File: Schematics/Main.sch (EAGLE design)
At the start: 12 parts, among them IC1 PIC12F1840, IC2 7805TV, Q1 BD139, X1 Fan, X2 Power

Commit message: All working now
Issues with repo resolved, back to normal!

Signed-off-by: Aljaž Srebrnič <a2piratesoft@gmail.com>
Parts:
- Q1: device transistor:-NPN-TO126 -> transistor-power:BD139
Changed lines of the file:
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@@
 <layers>
 <layer number="1" name="Top" color="4" fill="1" visible="no" active="no"/>
+<layer number="2" name="Route2" color="1" fill="3" visible="no" active="no"/>
+<layer number="3" name="Route3" color="4" fill="3" visible="no" active="no"/>
+<layer number="4" name="Route4" color="1" fill="4" visible="no" active="no"/>
+<layer number="5" name="Route5" color="4" fill="4" visible="no" active="no"/>
+<layer number="6" name="Route6" color="1" fill="8" visible="no" active="no"/>
+<layer number="7" name="Route7" color="4" fill="8" visible="no" active="no"/>
+<layer number="8" name="Route8" color="1" fill="2" visible="no" active="no"/>
+<layer number="9" name="Route9" color="4" fill="2" visible="no" active="no"/>
+<layer number="10" name="Route10" color="1" fill="7" visible="no" active="no"/>
+<layer number="11" name="Route11" color="4" fill="7" visible="no" active="no"/>
+<layer number="12" name="Route12" color="1" fill="5" visible="no" active="no"/>
+<layer number="13" name="Route13" color="4" fill="5" visible="no" active="no"/>
+<layer number="14" name="Route14" color="1" fill="6" visible="no" active="no"/>
+<layer number="15" name="Route15" color="4" fill="6" visible="no" active="no"/>
 <layer number="16" name="Bottom" color="1" fill="1" visible="no" active="no"/>
 <layer number="17" name="Pads" color="2" fill="1" visible="no" active="no"/>
@@
 <part name="IC1" library="microchip" deviceset="PIC12F6*" device="P" technology="29" value="PIC12F1840"/>
 <part name="IC2" library="linear" deviceset="78*" device="TV" technology="05"/>
-<part name="Q1" library="transistor" deviceset="*-NPN-" device="TO126" value="BD139"/>
+<part name="Q1" library="transistor-power" deviceset="BD139" device="" value="BD139"/>
 <part name="S1" library="switch" deviceset="55?" device="01"/>
 <part name="S2" library="switch" deviceset="55?" device="01"/>
@@
 </instance>
 <instance part="IC2" gate="A1" x="22.86" y="109.22"/>
-<instance part="Q1" gate="G$1" x="-2.54" y="68.58" rot="MR0"/>
+<instance part="Q1" gate="1" x="-2.54" y="68.58" rot="MR0"/>
 <instance part="S1" gate="G$1" x="68.58" y="81.28" rot="R90"/>
 <instance part="S2" gate="G$1" x="78.74" y="71.12" rot="R90"/>
@@
 <wire x1="-5.08" y1="73.66" x2="-5.08" y2="76.2" width="0.1524" layer="91"/>
 <wire x1="-5.08" y1="76.2" x2="-7.62" y2="76.2" width="0.1524" layer="91"/>
-<pinref part="Q1" gate="G$1" pin="C"/>
+<pinref part="Q1" gate="1" pin="C"/>
 <pinref part="X1" gate="-1" pin="S"/>
 </segment>
@@
 <segment>
 <wire x1="-5.08" y1="63.5" x2="-5.08" y2="58.42" width="0.1524" layer="91"/>
-<pinref part="Q1" gate="G$1" pin="E"/>
+<pinref part="Q1" gate="1" pin="E"/>
 <pinref part="GND3" gate="1" pin="GND"/>
 </segment>
@@
 <segment>
 <wire x1="5.08" y1="68.58" x2="0" y2="68.58" width="0.1524" layer="91"/>
-<pinref part="Q1" gate="G$1" pin="B"/>
+<pinref part="Q1" gate="1" pin="B"/>
 <pinref part="R2" gate="G$1" pin="1"/>
 </segment>

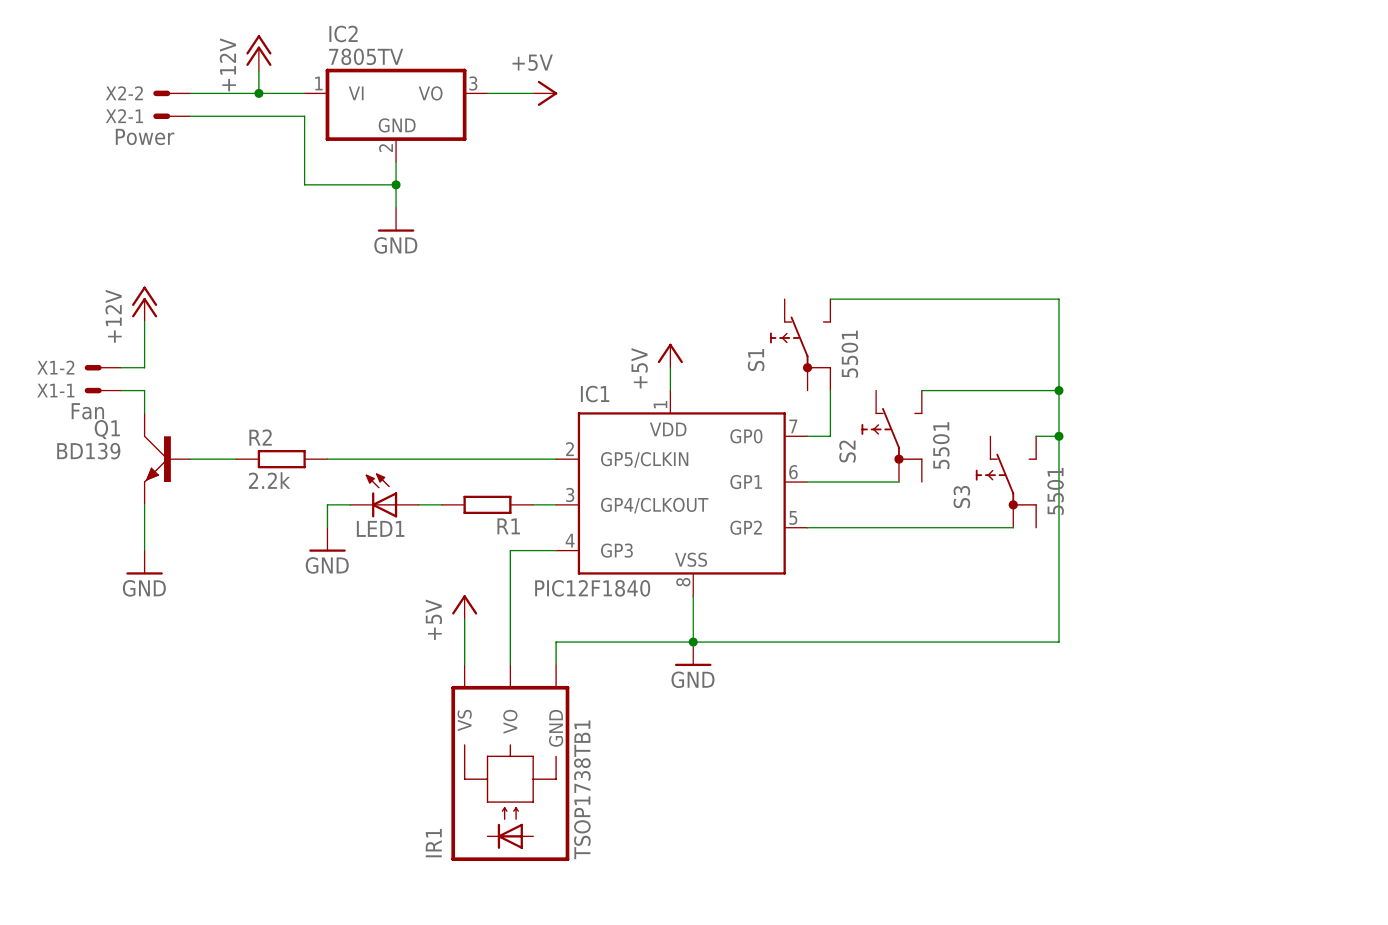
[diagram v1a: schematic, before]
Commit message: Ported schematics to next version of EAGLE
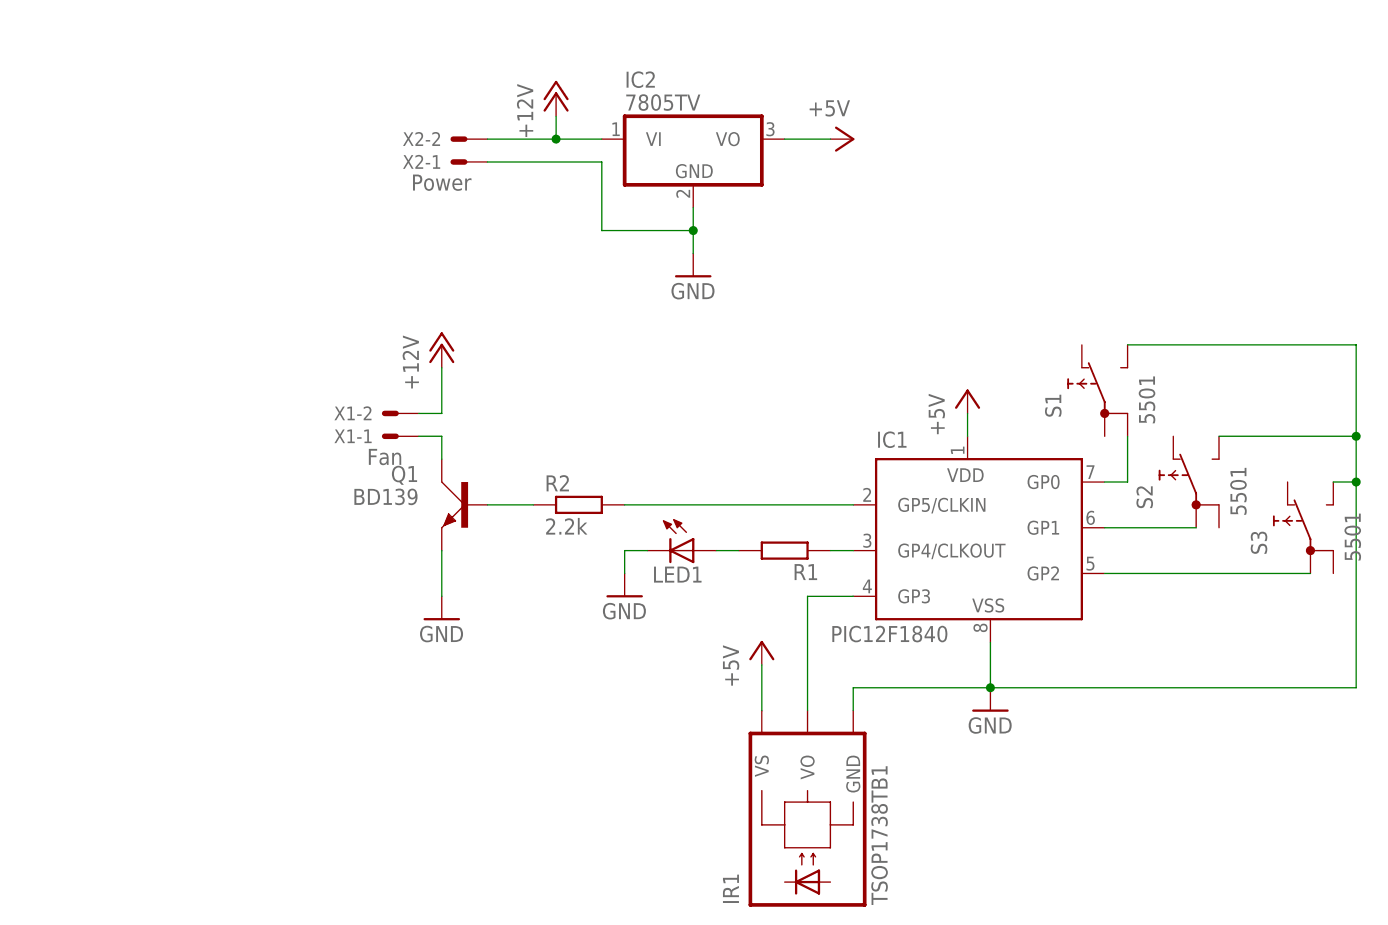
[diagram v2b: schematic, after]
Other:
- moved on the sheet: IC1, IC2, IR1, LED1, Q1, R1, R2, S1, S2, S3, X1-1, X1-2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
